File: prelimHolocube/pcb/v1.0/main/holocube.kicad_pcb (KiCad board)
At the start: 2 copper layers, 149 x 119 mm, 4 parts

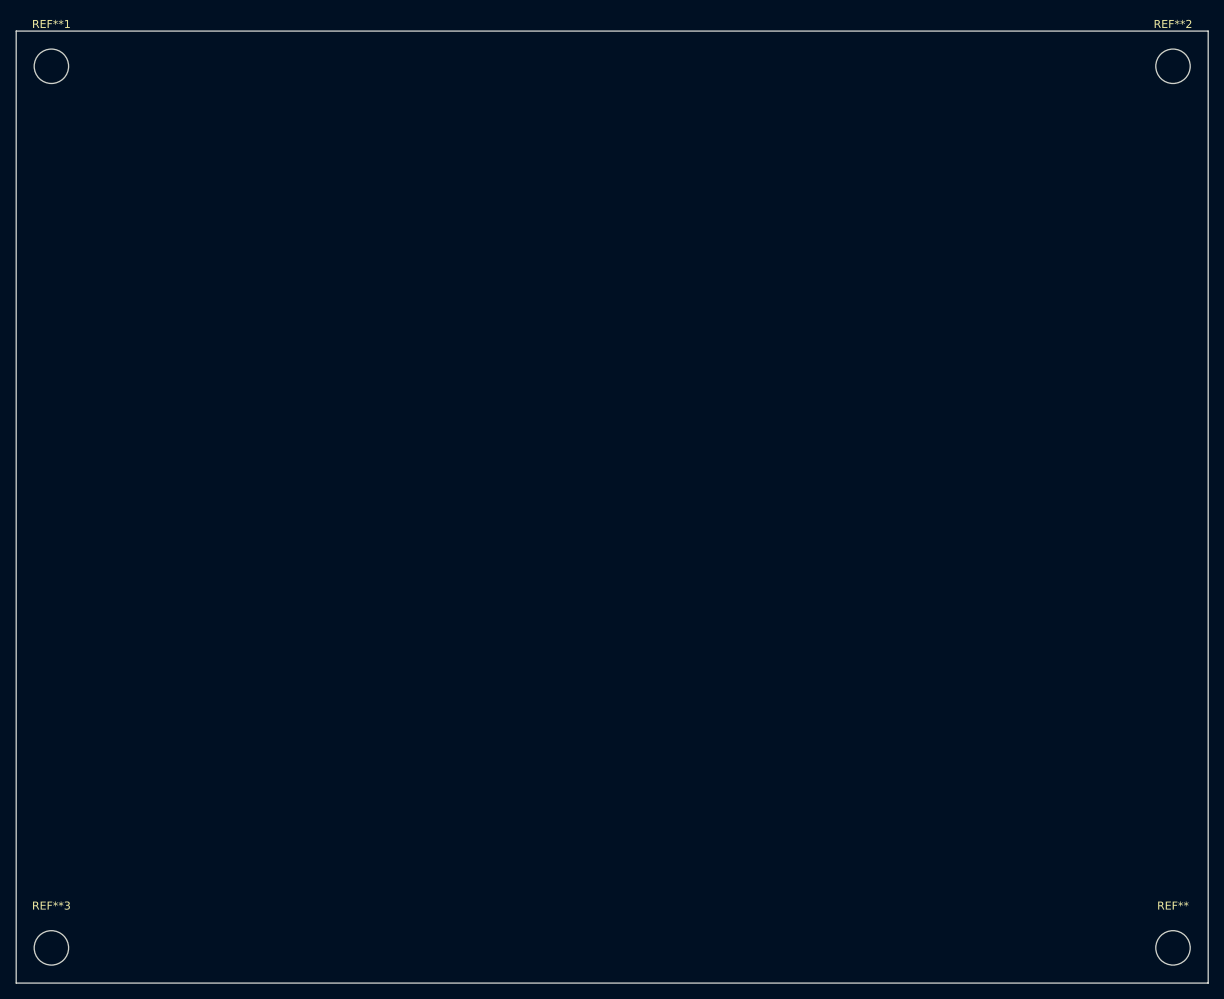
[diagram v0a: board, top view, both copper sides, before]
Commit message: Place v1.0 footprints on pcb and link 3d models
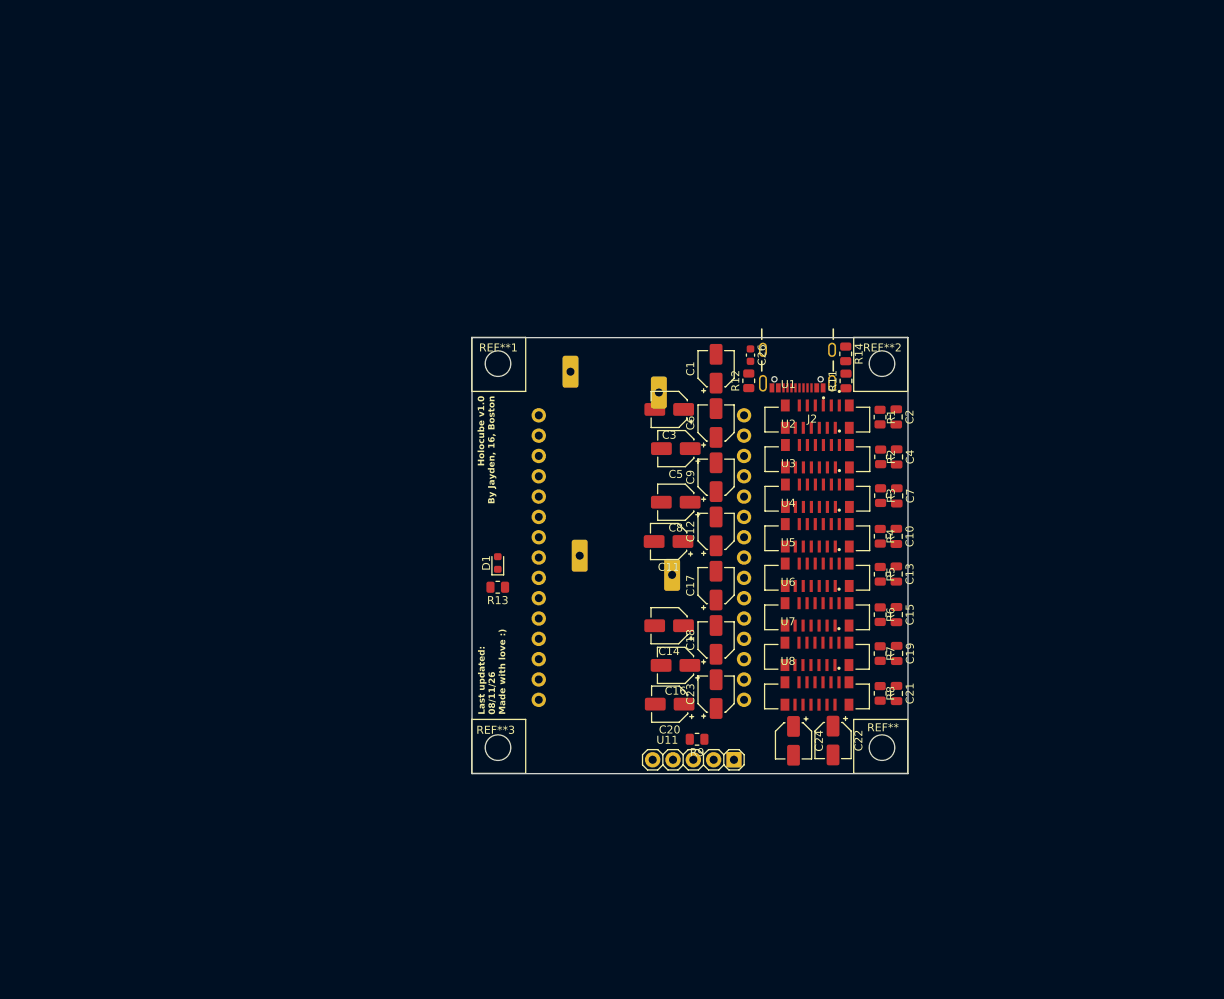
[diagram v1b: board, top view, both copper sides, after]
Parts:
- removed the REF** at (212.6, 146.3)
- added C1: 4.7uF, Capacitor_SMD:CP_Elec_4x5.4, F.Cu at (155.5, 73.9)
- added C10: 1uF ceramic, Capacitor_SMD:C_0805_2012Metric, F.Cu at (178.0, 94.8)
- added C11: 4.7uF, Capacitor_SMD:CP_Elec_4x5.4, F.Cu at (149.6, 95.5)
- added C12: 4.7uF, Capacitor_SMD:CP_Elec_4x5.4, F.Cu at (155.5, 94.2)
- added C13: 1uF ceramic, Capacitor_SMD:C_0805_2012Metric, F.Cu at (178.0, 99.5)
- added C14: 4.7uF, Capacitor_SMD:CP_Elec_4x5.4, F.Cu at (149.6, 106.0)
- added C15: 1uF ceramic, Capacitor_SMD:C_0805_2012Metric, F.Cu at (178.1, 104.6)
- added C16: 4.7uF, Capacitor_SMD:CP_Elec_4x5.4, F.Cu at (150.4, 111.0)
- added C17: 4.7uF, Capacitor_SMD:CP_Elec_4x5.4, F.Cu at (155.5, 101.0)
- added C18: 4.7uF, Capacitor_SMD:CP_Elec_4x5.4, F.Cu at (155.5, 107.8)
- added C19: 1uF ceramic, Capacitor_SMD:C_0805_2012Metric, F.Cu at (178.1, 109.5)
- added C2: 1uF ceramic, Capacitor_SMD:C_0805_2012Metric, F.Cu at (178.0, 79.9)
- added C20: 4.7uF, Capacitor_SMD:CP_Elec_4x5.4, F.Cu at (149.7, 115.8)
- added C21: 1uF ceramic, Capacitor_SMD:C_0805_2012Metric, F.Cu at (178.1, 114.5)
- added C22: 4.7uF, Capacitor_SMD:CP_Elec_4x5.4, F.Cu at (170.1, 120.4)
- added C23: 4.7uF, Capacitor_SMD:CP_Elec_4x5.4, F.Cu at (155.5, 114.6)
- added C24: 4.7uF, Capacitor_SMD:CP_Elec_4x5.4, F.Cu at (165.2, 120.4)
- added C26: 10nF 100V, Capacitor_SMD:C_0603_1608Metric, F.Cu at (159.8, 72.2)
- added C3: 4.7uF, Capacitor_SMD:CP_Elec_4x5.4, F.Cu at (149.7, 79.0)
- added C4: 1uF ceramic, Capacitor_SMD:C_0805_2012Metric, F.Cu at (178.1, 84.9)
- added C5: 4.7uF, Capacitor_SMD:CP_Elec_4x5.4, F.Cu at (150.5, 83.9)
- added C6: 4.7uF, Capacitor_SMD:CP_Elec_4x5.4, F.Cu at (155.5, 80.7)
- added C7: 1uF ceramic, Capacitor_SMD:C_0805_2012Metric, F.Cu at (178.1, 89.8)
- added C8: 4.7uF, Capacitor_SMD:CP_Elec_4x5.4, F.Cu at (150.5, 90.6)
- added C9: 4.7uF, Capacitor_SMD:CP_Elec_4x5.4, F.Cu at (155.5, 87.4)
- added D1: LED, LED_SMD:LED_0603_1608Metric, F.Cu at (128.2, 98.2)
- added J2: USB4105-GF-A, usbc_connector:usbc_connector, F.Cu at (165.7, 71.5)
- added R1: 1M, Resistor_SMD:R_0805_2012Metric, F.Cu at (176.0, 79.9)
- added R11: 5.1k 1%, Resistor_SMD:R_0805_2012Metric, F.Cu at (171.7, 75.4)
- added R12: 5.1k 1%, Resistor_SMD:R_0805_2012Metric, F.Cu at (159.6, 75.4)
- added R13: 68, Resistor_SMD:R_0805_2012Metric, F.Cu at (128.2, 101.2)
- added R14: 1M, Resistor_SMD:R_0805_2012Metric, F.Cu at (171.7, 72.0)
- added R2: 1M, Resistor_SMD:R_0805_2012Metric, F.Cu at (176.1, 84.9)
- added R3: 1M, Resistor_SMD:R_0805_2012Metric, F.Cu at (176.1, 89.7)
- added R4: 1M, Resistor_SMD:R_0805_2012Metric, F.Cu at (176.0, 94.8)
- added R5: 1M, Resistor_SMD:R_0805_2012Metric, F.Cu at (176.0, 99.6)
- added R6: 1M, Resistor_SMD:R_0805_2012Metric, F.Cu at (176.0, 104.6)
- added R7: 1M, Resistor_SMD:R_0805_2012Metric, F.Cu at (176.0, 109.5)
- added R8: 1M, Resistor_SMD:R_0805_2012Metric, F.Cu at (176.0, 114.5)
- added R9: 10k, Resistor_SMD:R_0805_2012Metric, F.Cu at (153.1, 120.2)
- added REF**: MountingHole_3.2mm_M3, MountingHole:MountingHole_3.2mm_M3, F.Cu at (176.2, 121.2)
- added U1: ~, Vertical_FPC-Connector_12P:AMPHENOL_F31W-1A7H1-11012, F.Cu at (168.2, 80.2)
- added U10: ~, boost_converter:Dorhea_MT3608_Adjustable, B.Cu at (143.7, 87.0)
- added U11: KY-040-PORT, KY-040:KY-040, F.Cu at (153.9, 122.8)
- added U2: ~, Vertical_FPC-Connector_12P:AMPHENOL_F31W-1A7H1-11012, F.Cu at (168.2, 85.2)
- added U3: ~, Vertical_FPC-Connector_12P:AMPHENOL_F31W-1A7H1-11012, F.Cu at (168.2, 90.1)
- added U4: ~, Vertical_FPC-Connector_12P:AMPHENOL_F31W-1A7H1-11012, F.Cu at (168.2, 95.1)
- added U5: ~, Vertical_FPC-Connector_12P:AMPHENOL_F31W-1A7H1-11012, F.Cu at (168.2, 100.0)
- added U6: ~, Vertical_FPC-Connector_12P:AMPHENOL_F31W-1A7H1-11012, F.Cu at (168.1, 105.0)
- added U7: ~, Vertical_FPC-Connector_12P:AMPHENOL_F31W-1A7H1-11012, F.Cu at (168.1, 109.9)
- added U8: ~, Vertical_FPC-Connector_12P:AMPHENOL_F31W-1A7H1-11012, F.Cu at (168.1, 114.9)
- added U9: ~, esp32:devkitv1-30pin, B.Cu at (146.2, 95.8)
- REF**1, REF**2, REF**3: value MountingHole_4.3mm_M4 -> MountingHole_3.2mm_M3; footprint MountingHole:MountingHole_4.3mm_M4 -> MountingHole:MountingHole_3.2mm_M3
- moved REF**1 67.1 mm to (128.2, 73.2)
- moved REF**3 61.2 mm to (128.2, 121.2)
- moved REF**2 52.0 mm to (176.2, 73.2)
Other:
- board size 149 x 119 mm -> 54.5 x 54.5 mm
- board text added: "Holocube v1.0 By Jayden, 16, Boston"
- board text added: "Last updated: 08/11/26 Made with love :)"

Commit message: order multiboard and update full board
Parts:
- removed R9: 10k, Resistor_SMD:R_0805_2012Metric
- U10: footprint boost_converter:Dorhea_MT3608_Adjustable -> boost_converter:HiLetgo_XL6009_Adjustable
- U11: value KY-040-PORT -> KY-040
- moved U10 10.4 mm to (146.2, 97.1), turned to -90 degrees
- moved REF** 0.18 mm to (176.1, 121.1)
- moved REF**1 0.18 mm to (128.4, 73.4)
- moved REF**2 0.18 mm to (176.1, 73.4)
- moved REF**3 0.18 mm to (128.4, 121.1)
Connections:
- U11 pad VCC: BOOST_IN -> +3.3V
- U9 pad 1: unconnected-(U9-VIN-Pad1) -> BOOST_IN
- U9 pad 13: Net-(U9-VN) -> unconnected-(U9-VN-Pad13)
- U9 pad 29: unconnected-(U9-D22-Pad29) -> KY_SW
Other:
- board text added: "Holocube v1.0 By Jayden, 17, Boston"
- board text added: "Last updated: 09/22/26 Made with love :)"
- board text removed: "Holocube v1.0 By Jayden, 16, Boston"
- board text removed: "Last updated: 08/11/26 Made with love :)"

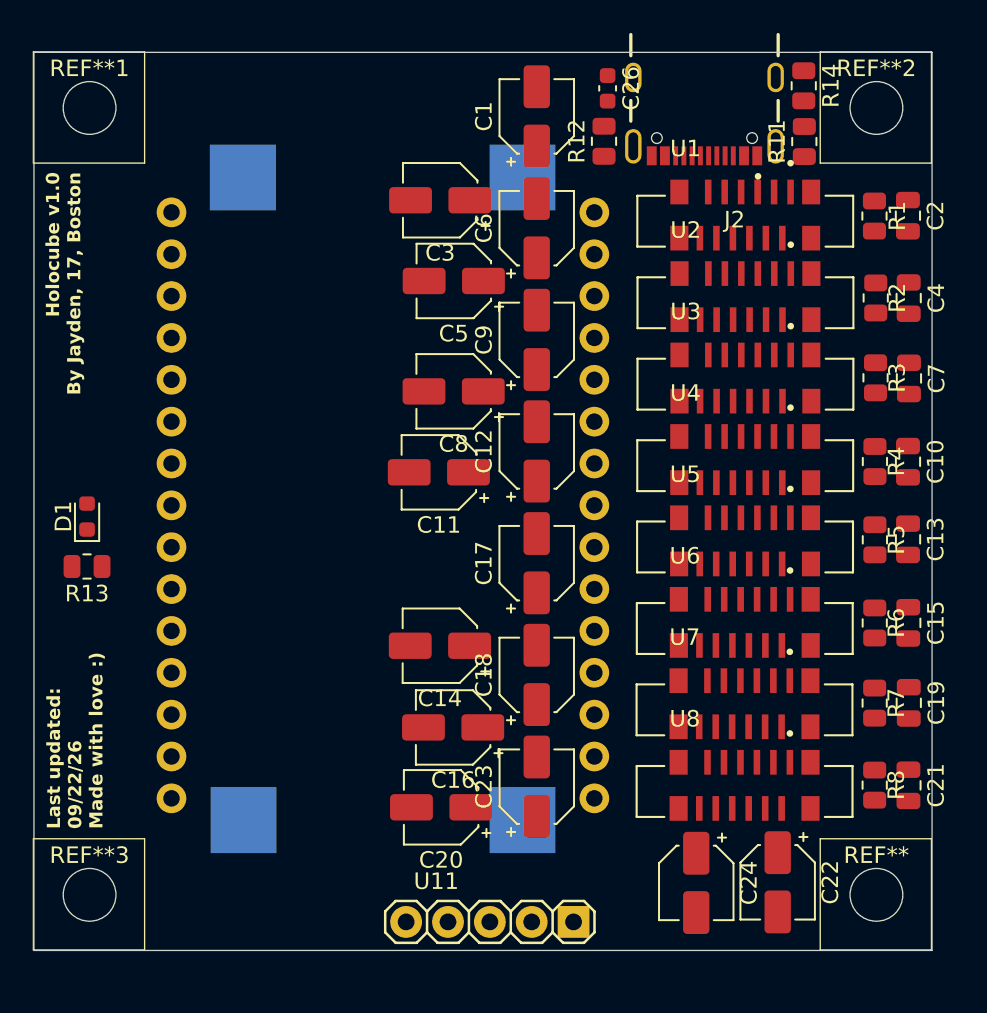
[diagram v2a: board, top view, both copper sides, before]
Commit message: lay routing foundation for main board v1.0
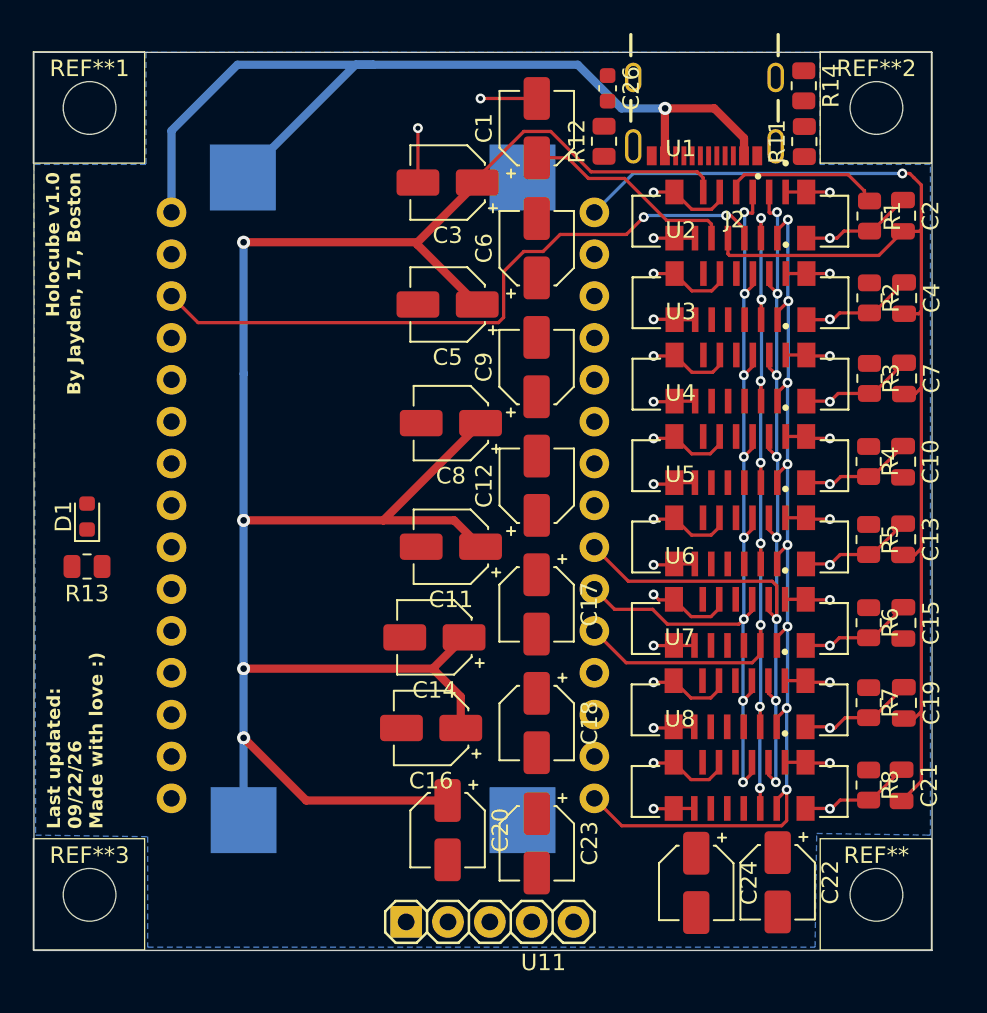
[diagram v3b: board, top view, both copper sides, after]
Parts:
- moved C11 4.57 mm to (150.3, 100.0)
- moved C23 3.44 mm to (155.5, 118.0), turned to -90 degrees
- moved C18 2.92 mm to (155.5, 110.7), turned to -90 degrees
- moved U11 2.54 mm to (151.4, 122.8), turned to 180 degrees
- moved C17 2.50 mm to (155.5, 103.5), turned to -90 degrees
- moved C12 2.08 mm to (155.5, 96.3)
- moved C8 1.94 mm to (150.3, 92.5)
- moved C9 1.65 mm to (155.5, 89.1)
- moved C5 1.47 mm to (150.1, 85.3)
- moved C20 1.44 mm to (150.1, 117.2), turned to -90 degrees
- moved C16 1.34 mm to (149.1, 111.0)
- moved C6 1.21 mm to (155.5, 81.9)
- moved C3 1.16 mm to (150.1, 77.9)
- moved C1 0.71 mm to (155.5, 74.6)
- moved C14 0.61 mm to (149.3, 105.5)
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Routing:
- net GND: track 0.00 -> 145.6 mm, vias 0 -> 34
- net +13.5V: track 0.00 -> 129.2 mm, vias 0 -> 4
- net +3.3V: track 0.00 -> 77.2 mm, vias 0 -> 1
- net SCL: track 0.00 -> 60.3 mm, vias 0 -> 8
- net SI: track 0.00 -> 60.1 mm, vias 0 -> 8
- net BOOST_IN: track 0.00 -> 57.9 mm, vias 0 -> 1
- net A0: track 0.00 -> 57.4 mm, vias 0 -> 8
- net RES: track 0.00 -> 56.6 mm, vias 0 -> 8
- net CS1: track 0.00 -> 40.6 mm, vias 0 -> 2
- net Net-(U1-VCOMH): track 0.00 -> 13.1 mm
- net Net-(U1-IREF): track 0.00 -> 9.70 mm
- added copper zone on B.Cu, net GND
